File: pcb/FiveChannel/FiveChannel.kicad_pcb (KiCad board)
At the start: 2 copper layers, 79.8 x 76 mm, 29 parts, among them J101 UPDI, J102 5V In, J201 Power Out, J202 NeoPixel Data, J203 Power Out, J204 NeoPixel Data, J205 Power Out, J206 NeoPixel Data, J207 Power Out, J208 NeoPixel Data, J209 Power Out, J210 NeoPixel Data, U101 74LS596, U102 ATTINY1614

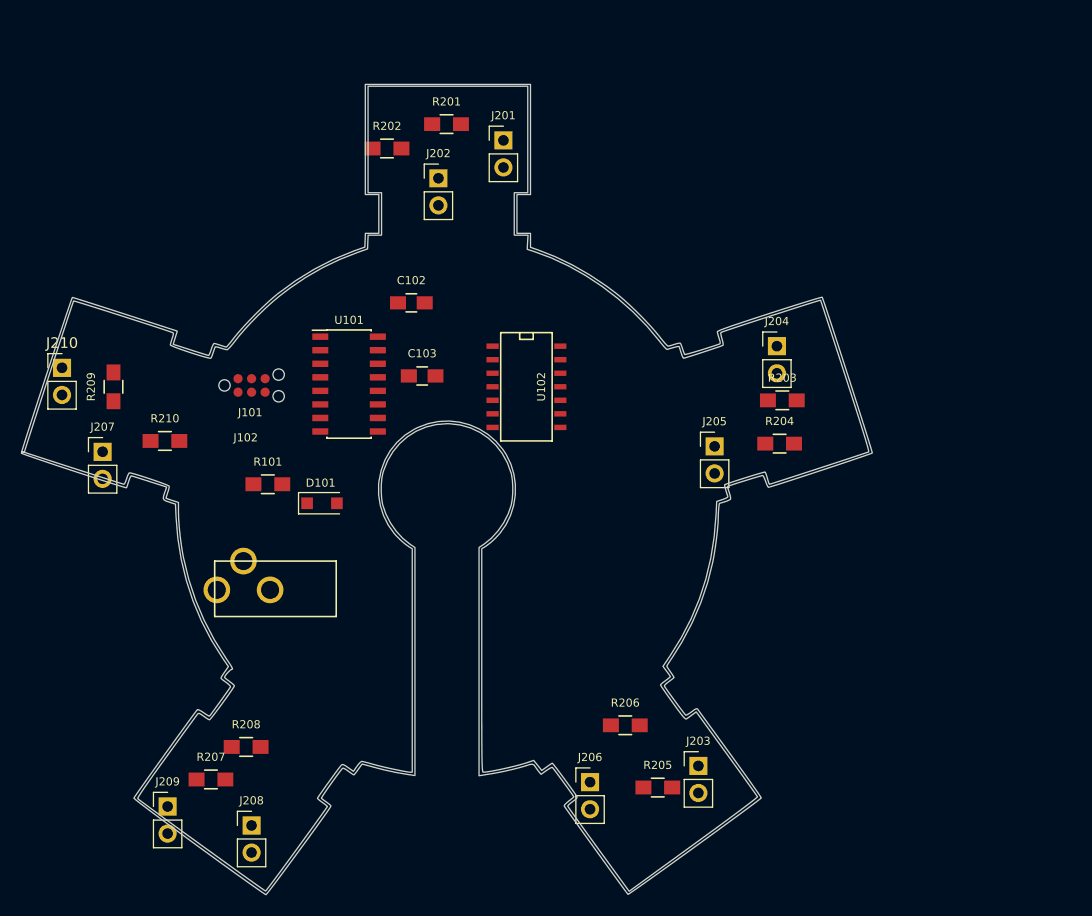
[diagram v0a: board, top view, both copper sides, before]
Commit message: Working through the five channel prototype layout
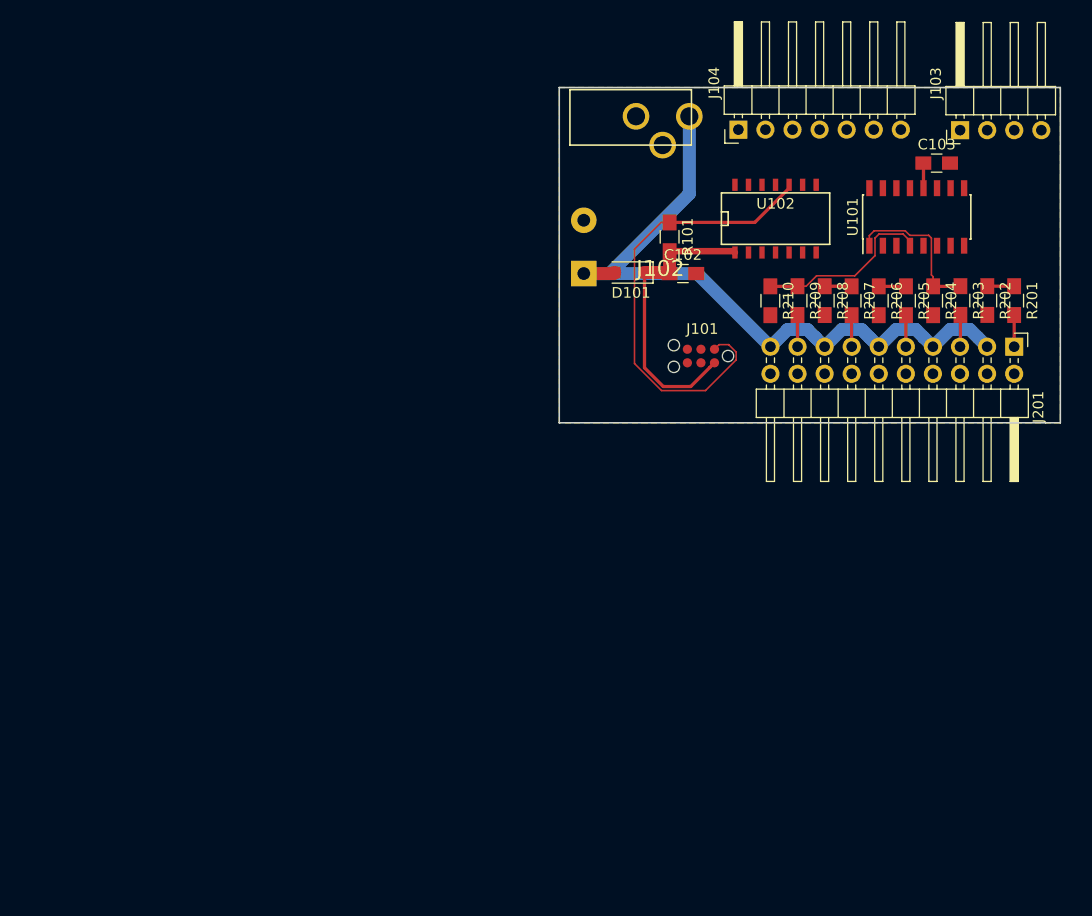
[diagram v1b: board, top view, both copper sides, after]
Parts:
- removed G***: LOGO, advent_sternla:EdgeCut_5
- removed J202, J204, J206, J208, J210: NeoPixel Data, Pin_Headers:Pin_Header_Straight_1x02_Pitch2.54mm
- removed J203, J205, J207, J209: Power Out, Pin_Headers:Pin_Header_Straight_1x02_Pitch2.54mm
- added C101: 1000μF 25V, advent_sternla:CP_Radial_L21.0mm_D13.0mm_P5.00mm_Horizontal, B.Cu at (128.9, 64.3)
- added J103: Conn_01x04_Male, Pin_Headers:Pin_Header_Angled_1x04_Pitch2.54mm, F.Cu at (164.2, 53.4)
- added J104: Conn_01x07_Male, Pin_Headers:Pin_Header_Angled_1x07_Pitch2.54mm, F.Cu at (143.4, 53.4)
- J201: value Power Out -> Conn_01x20_Male; footprint Pin_Headers:Pin_Header_Straight_1x02_Pitch2.54mm -> Pin_Headers:Pin_Header_Angled_2x10_Pitch2.54mm
- moved R207 75.0 mm to (154.1, 69.4), turned to 270 degrees
- moved R208 68.5 mm to (151.6, 69.4), turned to 270 degrees
- moved R209 64.7 mm to (149.0, 69.4), turned to 270 degrees
- moved J102 59.3 mm to (136.3, 52.1), turned to 0 degrees
- moved R210 58.3 mm to (146.4, 69.4), turned to 270 degrees
- moved R202 58.1 mm to (166.8, 69.4), turned to 270 degrees
- moved R201 55.8 mm to (169.3, 69.4), turned to 270 degrees
- moved U101 55.5 mm to (160.2, 61.5), turned to 90 degrees
- moved C103 52.2 mm to (162.1, 56.5)
- moved J201 51.7 mm to (169.3, 73.7), turned to 270 degrees
- moved R205 51.3 mm to (159.2, 69.4), turned to 270 degrees
- moved R206 46.4 mm to (156.6, 69.4), turned to 270 degrees
- moved J101 44.9 mm to (141.2, 73.9), turned to 180 degrees
- moved R101 44.3 mm to (137.0, 63.4), turned to 270 degrees
- moved D101 36.1 mm to (133.2, 66.8), turned to 180 degrees
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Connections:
- J201 pad 1: /VDD -> /Channels/NP_DATA_0
- U102 pad 3: (no net) -> /PA5
- U102 pad 4: (no net) -> /PA6
- U102 pad 5: (no net) -> /PA7
- U102 pad 6: (no net) -> /PB3
- U102 pad 7: (no net) -> /PB2
- U102 pad 8: (no net) -> /PB1
- U102 pad 9: (no net) -> /PB0
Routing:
- net /5V: track 0.00 -> 69.2 mm
- net /PDI_DATA: track 0.00 -> 43.0 mm
- net /VDD: track 0.00 -> 27.8 mm
- net /CHANNEL_4: track 0.00 -> 16.8 mm
- net /CHANNEL_1: track 0.00 -> 14.4 mm
- net /CHANNEL_3: track 0.00 -> 3.38 mm
- net /CHANNEL_2: track 0.00 -> 3.09 mm
- net /Channels/NP_DATA_1: track 0.00 -> 3.05 mm
- net /Channels/NP_DATA_3: track 0.00 -> 2.98 mm
- net /Channels/NP_DATA_2: track 0.00 -> 2.98 mm
- net /Channels/NP_DATA_4: track 0.00 -> 2.97 mm
- net /Channels/NP_DATA_0: track 0.00 -> 2.97 mm
- net /CHANNEL_0: track 0.00 -> 2.52 mm
- net /LATCH_PIN: track 0.00 -> 2.36 mm
- added copper zone on F.Cu, net GND
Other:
- board size 79.8 x 76 mm -> 47 x 31.4 mm

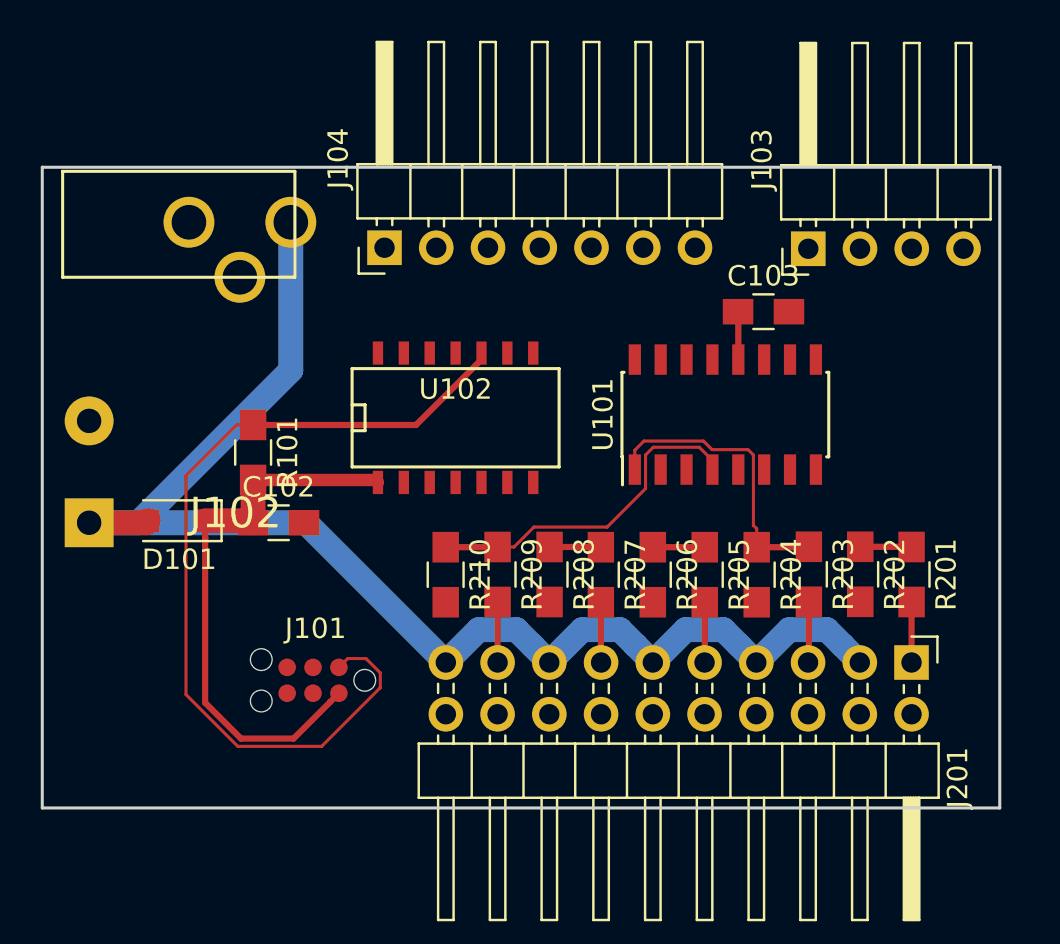
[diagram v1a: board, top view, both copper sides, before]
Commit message: Finished the layout and sent to OSH Park
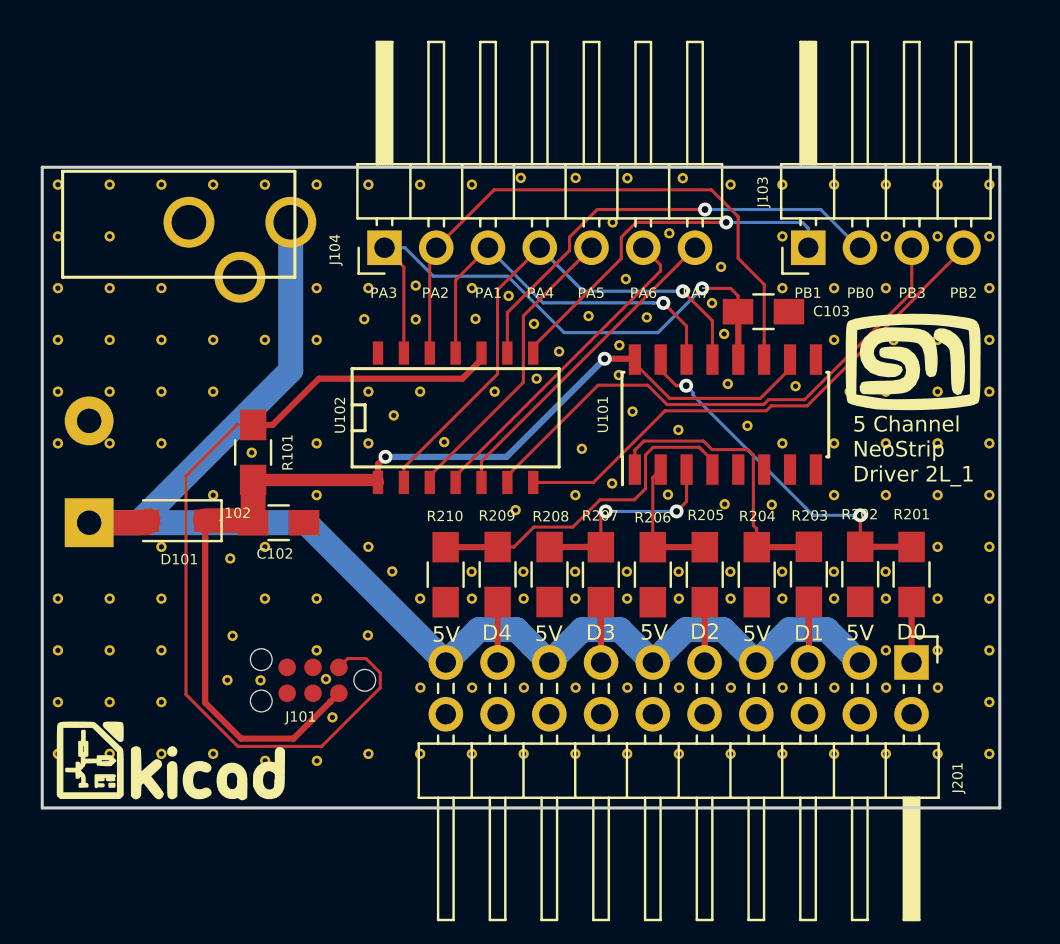
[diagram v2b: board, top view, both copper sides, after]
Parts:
- added G***: LOGO, advent_sternla:MyBasic_rounded_50_1, B.Cu at (157.0, 64.3)
- added G***: LOGO, advent_sternla:KiCad-Logo, F.Cu at (133.0, 78.5)
- added G***: LOGO, advent_sternla:MyBasic_rounded_50_1, F.Cu at (169.4, 58.9)
- added REF***: KiCad-Logo2_6mm_SilkScreen, Symbols:KiCad-Logo2_6mm_SilkScreen, B.Cu at (169.6, 64.2)
- added ST**: STITCH_VIA, advent_sternla:STITCH_VIA, F.Cu at (135.7, 74.6)
- added ST**: STITCH_VIA, advent_sternla:STITCH_VIA, F.Cu at (157.9, 78.2)
- added ST**: STITCH_VIA, advent_sternla:STITCH_VIA, F.Cu at (161.3, 62.1)
- added ST**: STITCH_VIA, advent_sternla:STITCH_VIA, F.Cu at (157.9, 62.3)
- added ST**: STITCH_VIA, advent_sternla:STITCH_VIA, F.Cu at (155.6, 61.4)
- added ST**: STITCH_VIA, advent_sternla:STITCH_VIA, F.Cu at (153.1, 63.2)
- added ST**: STITCH_VIA, advent_sternla:STITCH_VIA, F.Cu at (146.4, 62.9)
- added ST**: STITCH_VIA, advent_sternla:STITCH_VIA, F.Cu at (142.7, 63.0)
- added ST**: STITCH_VIA, advent_sternla:STITCH_VIA, F.Cu at (140.1, 63.0)
- added ST**: STITCH_VIA, advent_sternla:STITCH_VIA, F.Cu at (136.9, 63.4)
- added ST**: STITCH_VIA, advent_sternla:STITCH_VIA, F.Cu at (132.5, 63.0)
- added ST**: STITCH_VIA, advent_sternla:STITCH_VIA, F.Cu at (130.0, 63.0)
- added ST**: STITCH_VIA, advent_sternla:STITCH_VIA, F.Cu at (155.4, 78.2)
- added ST**: STITCH_VIA, advent_sternla:STITCH_VIA, F.Cu at (127.4, 63.0)
- added ST**: STITCH_VIA, advent_sternla:STITCH_VIA, F.Cu at (173.1, 60.4)
- added ST**: STITCH_VIA, advent_sternla:STITCH_VIA, F.Cu at (170.6, 60.4)
- added ST**: STITCH_VIA, advent_sternla:STITCH_VIA, F.Cu at (168.1, 60.4)
- added ST**: STITCH_VIA, advent_sternla:STITCH_VIA, F.Cu at (166.3, 60.4)
- added ST**: STITCH_VIA, advent_sternla:STITCH_VIA, F.Cu at (163.6, 60.1)
- added ST**: STITCH_VIA, advent_sternla:STITCH_VIA, F.Cu at (160.3, 60.0)
- added ST**: STITCH_VIA, advent_sternla:STITCH_VIA, F.Cu at (150.9, 59.8)
- added ST**: STITCH_VIA, advent_sternla:STITCH_VIA, F.Cu at (148.9, 60.4)
- added ST**: STITCH_VIA, advent_sternla:STITCH_VIA, F.Cu at (145.2, 60.4)
- added ST**: STITCH_VIA, advent_sternla:STITCH_VIA, F.Cu at (152.8, 78.2)
- added ST**: STITCH_VIA, advent_sternla:STITCH_VIA, F.Cu at (142.7, 60.4)
- added ST**: STITCH_VIA, advent_sternla:STITCH_VIA, F.Cu at (135.0, 60.4)
- added ST**: STITCH_VIA, advent_sternla:STITCH_VIA, F.Cu at (132.5, 60.4)
- added ST**: STITCH_VIA, advent_sternla:STITCH_VIA, F.Cu at (130.0, 60.4)
- added ST**: STITCH_VIA, advent_sternla:STITCH_VIA, F.Cu at (127.4, 60.4)
- added ST**: STITCH_VIA, advent_sternla:STITCH_VIA, F.Cu at (173.1, 57.9)
- added ST**: STITCH_VIA, advent_sternla:STITCH_VIA, F.Cu at (170.6, 57.9)
- added ST**: STITCH_VIA, advent_sternla:STITCH_VIA, F.Cu at (168.4, 57.9)
- added ST**: STITCH_VIA, advent_sternla:STITCH_VIA, F.Cu at (165.5, 57.9)
- added ST**: STITCH_VIA, advent_sternla:STITCH_VIA, F.Cu at (160.1, 57.6)
- added ST**: STITCH_VIA, advent_sternla:STITCH_VIA, F.Cu at (150.3, 78.2)
- added ST**: STITCH_VIA, advent_sternla:STITCH_VIA, F.Cu at (155.0, 58.1)
- added ST**: STITCH_VIA, advent_sternla:STITCH_VIA, F.Cu at (152.0, 58.4)
- added ST**: STITCH_VIA, advent_sternla:STITCH_VIA, F.Cu at (150.8, 57.1)
- added ST**: STITCH_VIA, advent_sternla:STITCH_VIA, F.Cu at (147.9, 56.8)
- added ST**: STITCH_VIA, advent_sternla:STITCH_VIA, F.Cu at (145.0, 56.9)
- added ST**: STITCH_VIA, advent_sternla:STITCH_VIA, F.Cu at (142.5, 56.9)
- added ST**: STITCH_VIA, advent_sternla:STITCH_VIA, F.Cu at (140.1, 57.9)
- added ST**: STITCH_VIA, advent_sternla:STITCH_VIA, F.Cu at (137.6, 57.9)
- added ST**: STITCH_VIA, advent_sternla:STITCH_VIA, F.Cu at (135.0, 57.9)
- added ST**: STITCH_VIA, advent_sternla:STITCH_VIA, F.Cu at (132.5, 57.9)
- added ST**: STITCH_VIA, advent_sternla:STITCH_VIA, F.Cu at (147.7, 78.2)
- added ST**: STITCH_VIA, advent_sternla:STITCH_VIA, F.Cu at (130.0, 57.9)
- added ST**: STITCH_VIA, advent_sternla:STITCH_VIA, F.Cu at (127.4, 57.9)
- added ST**: STITCH_VIA, advent_sternla:STITCH_VIA, F.Cu at (173.1, 55.3)
- added ST**: STITCH_VIA, advent_sternla:STITCH_VIA, F.Cu at (168.1, 55.3)
- added ST**: STITCH_VIA, advent_sternla:STITCH_VIA, F.Cu at (165.5, 55.3)
- added ST**: STITCH_VIA, advent_sternla:STITCH_VIA, F.Cu at (163.0, 55.3)
- added ST**: STITCH_VIA, advent_sternla:STITCH_VIA, F.Cu at (159.5, 56.1)
- added ST**: STITCH_VIA, advent_sternla:STITCH_VIA, F.Cu at (156.3, 56.8)
- added ST**: STITCH_VIA, advent_sternla:STITCH_VIA, F.Cu at (155.3, 54.9)
- added ST**: STITCH_VIA, advent_sternla:STITCH_VIA, F.Cu at (153.5, 56.7)
- added ST**: STITCH_VIA, advent_sternla:STITCH_VIA, F.Cu at (145.2, 78.2)
- added ST**: STITCH_VIA, advent_sternla:STITCH_VIA, F.Cu at (149.5, 55.7)
- added ST**: STITCH_VIA, advent_sternla:STITCH_VIA, F.Cu at (147.7, 55.3)
- added ST**: STITCH_VIA, advent_sternla:STITCH_VIA, F.Cu at (145.0, 55.2)
- added ST**: STITCH_VIA, advent_sternla:STITCH_VIA, F.Cu at (142.7, 55.3)
- added ST**: STITCH_VIA, advent_sternla:STITCH_VIA, F.Cu at (140.1, 55.3)
- added ST**: STITCH_VIA, advent_sternla:STITCH_VIA, F.Cu at (154.6, 52.1)
- added ST**: STITCH_VIA, advent_sternla:STITCH_VIA, F.Cu at (157.4, 52.6)
- added ST**: STITCH_VIA, advent_sternla:STITCH_VIA, F.Cu at (132.5, 55.3)
- added ST**: STITCH_VIA, advent_sternla:STITCH_VIA, F.Cu at (130.0, 55.3)
- added ST**: STITCH_VIA, advent_sternla:STITCH_VIA, F.Cu at (127.4, 55.3)
- added ST**: STITCH_VIA, advent_sternla:STITCH_VIA, F.Cu at (142.7, 78.2)
- added ST**: STITCH_VIA, advent_sternla:STITCH_VIA, F.Cu at (173.1, 52.8)
- added ST**: STITCH_VIA, advent_sternla:STITCH_VIA, F.Cu at (170.6, 52.8)
- added ST**: STITCH_VIA, advent_sternla:STITCH_VIA, F.Cu at (168.1, 52.8)
- added ST**: STITCH_VIA, advent_sternla:STITCH_VIA, F.Cu at (163.0, 52.8)
- added ST**: STITCH_VIA, advent_sternla:STITCH_VIA, F.Cu at (160.0, 54.3)
- added ST**: STITCH_VIA, advent_sternla:STITCH_VIA, F.Cu at (130.0, 52.8)
- added ST**: STITCH_VIA, advent_sternla:STITCH_VIA, F.Cu at (127.4, 52.8)
- added ST**: STITCH_VIA, advent_sternla:STITCH_VIA, F.Cu at (173.1, 50.3)
- added ST**: STITCH_VIA, advent_sternla:STITCH_VIA, F.Cu at (170.6, 50.3)
- added ST**: STITCH_VIA, advent_sternla:STITCH_VIA, F.Cu at (168.1, 50.3)
- added ST**: STITCH_VIA, advent_sternla:STITCH_VIA, F.Cu at (140.1, 78.5)
- added ST**: STITCH_VIA, advent_sternla:STITCH_VIA, F.Cu at (165.5, 50.3)
- added ST**: STITCH_VIA, advent_sternla:STITCH_VIA, F.Cu at (163.0, 50.3)
- added ST**: STITCH_VIA, advent_sternla:STITCH_VIA, F.Cu at (160.4, 50.3)
- added ST**: STITCH_VIA, advent_sternla:STITCH_VIA, F.Cu at (158.1, 49.9)
- added ST**: STITCH_VIA, advent_sternla:STITCH_VIA, F.Cu at (155.4, 49.9)
- added ST**: STITCH_VIA, advent_sternla:STITCH_VIA, F.Cu at (152.8, 49.9)
- added ST**: STITCH_VIA, advent_sternla:STITCH_VIA, F.Cu at (150.1, 49.9)
- added ST**: STITCH_VIA, advent_sternla:STITCH_VIA, F.Cu at (147.7, 50.3)
- added ST**: STITCH_VIA, advent_sternla:STITCH_VIA, F.Cu at (145.2, 50.3)
- added ST**: STITCH_VIA, advent_sternla:STITCH_VIA, F.Cu at (142.7, 50.3)
- added ST**: STITCH_VIA, advent_sternla:STITCH_VIA, F.Cu at (137.6, 78.5)
- added ST**: STITCH_VIA, advent_sternla:STITCH_VIA, F.Cu at (140.1, 50.3)
- added ST**: STITCH_VIA, advent_sternla:STITCH_VIA, F.Cu at (137.6, 50.3)
- added ST**: STITCH_VIA, advent_sternla:STITCH_VIA, F.Cu at (135.0, 50.3)
- added ST**: STITCH_VIA, advent_sternla:STITCH_VIA, F.Cu at (132.5, 50.3)
- added ST**: STITCH_VIA, advent_sternla:STITCH_VIA, F.Cu at (130.0, 50.3)
- added ST**: STITCH_VIA, advent_sternla:STITCH_VIA, F.Cu at (127.4, 50.3)
- added ST**: STITCH_VIA, advent_sternla:STITCH_VIA, F.Cu at (135.0, 78.2)
- added ST**: STITCH_VIA, advent_sternla:STITCH_VIA, F.Cu at (155.0, 59.6)
- added ST**: STITCH_VIA, advent_sternla:STITCH_VIA, F.Cu at (132.5, 78.2)
- added ST**: STITCH_VIA, advent_sternla:STITCH_VIA, F.Cu at (130.0, 78.2)
- added ST**: STITCH_VIA, advent_sternla:STITCH_VIA, F.Cu at (127.4, 78.2)
- added ST**: STITCH_VIA, advent_sternla:STITCH_VIA, F.Cu at (173.1, 75.7)
- added ST**: STITCH_VIA, advent_sternla:STITCH_VIA, F.Cu at (170.6, 74.9)
- added ST**: STITCH_VIA, advent_sternla:STITCH_VIA, F.Cu at (168.1, 74.9)
- added ST**: STITCH_VIA, advent_sternla:STITCH_VIA, F.Cu at (165.5, 74.9)
- added ST**: STITCH_VIA, advent_sternla:STITCH_VIA, F.Cu at (163.0, 74.9)
- added ST**: STITCH_VIA, advent_sternla:STITCH_VIA, F.Cu at (160.5, 74.9)
- added ST**: STITCH_VIA, advent_sternla:STITCH_VIA, F.Cu at (157.9, 74.9)
- added ST**: STITCH_VIA, advent_sternla:STITCH_VIA, F.Cu at (143.9, 61.6)
- added ST**: STITCH_VIA, advent_sternla:STITCH_VIA, F.Cu at (155.4, 74.9)
- added ST**: STITCH_VIA, advent_sternla:STITCH_VIA, F.Cu at (152.8, 74.9)
- added ST**: STITCH_VIA, advent_sternla:STITCH_VIA, F.Cu at (150.3, 74.9)
- added ST**: STITCH_VIA, advent_sternla:STITCH_VIA, F.Cu at (147.8, 74.9)
- added ST**: STITCH_VIA, advent_sternla:STITCH_VIA, F.Cu at (145.2, 74.9)
- added ST**: STITCH_VIA, advent_sternla:STITCH_VIA, F.Cu at (140.9, 76.4)
- added ST**: STITCH_VIA, advent_sternla:STITCH_VIA, F.Cu at (140.6, 74.5)
- added ST**: STITCH_VIA, advent_sternla:STITCH_VIA, F.Cu at (136.0, 72.4)
- added ST**: STITCH_VIA, advent_sternla:STITCH_VIA, F.Cu at (132.5, 75.7)
- added ST**: STITCH_VIA, advent_sternla:STITCH_VIA, F.Cu at (130.0, 75.7)
- added ST**: STITCH_VIA, advent_sternla:STITCH_VIA, F.Cu at (173.1, 78.2)
- added ST**: STITCH_VIA, advent_sternla:STITCH_VIA, F.Cu at (127.4, 75.7)
- added ST**: STITCH_VIA, advent_sternla:STITCH_VIA, F.Cu at (173.1, 73.1)
- added ST**: STITCH_VIA, advent_sternla:STITCH_VIA, F.Cu at (170.6, 73.1)
- added ST**: STITCH_VIA, advent_sternla:STITCH_VIA, F.Cu at (168.1, 73.1)
- added ST**: STITCH_VIA, advent_sternla:STITCH_VIA, F.Cu at (142.6, 72.4)
- added ST**: STITCH_VIA, advent_sternla:STITCH_VIA, F.Cu at (140.1, 73.1)
- added ST**: STITCH_VIA, advent_sternla:STITCH_VIA, F.Cu at (137.4, 74.6)
- added ST**: STITCH_VIA, advent_sternla:STITCH_VIA, F.Cu at (132.5, 73.1)
- added ST**: STITCH_VIA, advent_sternla:STITCH_VIA, F.Cu at (130.0, 73.1)
- added ST**: STITCH_VIA, advent_sternla:STITCH_VIA, F.Cu at (127.4, 73.1)
- added ST**: STITCH_VIA, advent_sternla:STITCH_VIA, F.Cu at (170.6, 78.2)
- added ST**: STITCH_VIA, advent_sternla:STITCH_VIA, F.Cu at (173.1, 70.6)
- added ST**: STITCH_VIA, advent_sternla:STITCH_VIA, F.Cu at (170.6, 70.6)
- added ST**: STITCH_VIA, advent_sternla:STITCH_VIA, F.Cu at (168.1, 70.6)
- added ST**: STITCH_VIA, advent_sternla:STITCH_VIA, F.Cu at (165.5, 70.6)
- added ST**: STITCH_VIA, advent_sternla:STITCH_VIA, F.Cu at (163.0, 70.6)
- added ST**: STITCH_VIA, advent_sternla:STITCH_VIA, F.Cu at (160.4, 70.6)
- added ST**: STITCH_VIA, advent_sternla:STITCH_VIA, F.Cu at (157.9, 70.6)
- added ST**: STITCH_VIA, advent_sternla:STITCH_VIA, F.Cu at (155.4, 70.6)
- added ST**: STITCH_VIA, advent_sternla:STITCH_VIA, F.Cu at (152.8, 70.6)
- added ST**: STITCH_VIA, advent_sternla:STITCH_VIA, F.Cu at (150.3, 70.6)
- added ST**: STITCH_VIA, advent_sternla:STITCH_VIA, F.Cu at (168.1, 78.2)
- added ST**: STITCH_VIA, advent_sternla:STITCH_VIA, F.Cu at (147.7, 70.6)
- added ST**: STITCH_VIA, advent_sternla:STITCH_VIA, F.Cu at (145.2, 70.6)
- added ST**: STITCH_VIA, advent_sternla:STITCH_VIA, F.Cu at (140.1, 70.6)
- added ST**: STITCH_VIA, advent_sternla:STITCH_VIA, F.Cu at (137.6, 70.6)
- added ST**: STITCH_VIA, advent_sternla:STITCH_VIA, F.Cu at (132.5, 70.6)
- added ST**: STITCH_VIA, advent_sternla:STITCH_VIA, F.Cu at (130.0, 70.6)
- added ST**: STITCH_VIA, advent_sternla:STITCH_VIA, F.Cu at (127.4, 70.6)
- added ST**: STITCH_VIA, advent_sternla:STITCH_VIA, F.Cu at (173.1, 68.0)
- added ST**: STITCH_VIA, advent_sternla:STITCH_VIA, F.Cu at (170.6, 68.0)
- added ST**: STITCH_VIA, advent_sternla:STITCH_VIA, F.Cu at (168.0, 69.3)
- added ST**: STITCH_VIA, advent_sternla:STITCH_VIA, F.Cu at (165.5, 78.2)
- added ST**: STITCH_VIA, advent_sternla:STITCH_VIA, F.Cu at (165.5, 69.3)
- added ST**: STITCH_VIA, advent_sternla:STITCH_VIA, F.Cu at (163.0, 69.3)
- added ST**: STITCH_VIA, advent_sternla:STITCH_VIA, F.Cu at (160.4, 69.3)
- added ST**: STITCH_VIA, advent_sternla:STITCH_VIA, F.Cu at (157.9, 69.3)
- added ST**: STITCH_VIA, advent_sternla:STITCH_VIA, F.Cu at (155.3, 69.3)
- added ST**: STITCH_VIA, advent_sternla:STITCH_VIA, F.Cu at (152.8, 69.3)
- added ST**: STITCH_VIA, advent_sternla:STITCH_VIA, F.Cu at (150.3, 69.3)
- added ST**: STITCH_VIA, advent_sternla:STITCH_VIA, F.Cu at (147.7, 69.3)
- added ST**: STITCH_VIA, advent_sternla:STITCH_VIA, F.Cu at (143.8, 69.2)
- added ST**: STITCH_VIA, advent_sternla:STITCH_VIA, F.Cu at (142.7, 68.0)
- added ST**: STITCH_VIA, advent_sternla:STITCH_VIA, F.Cu at (163.0, 78.2)
- added ST**: STITCH_VIA, advent_sternla:STITCH_VIA, F.Cu at (137.6, 68.0)
- added ST**: STITCH_VIA, advent_sternla:STITCH_VIA, F.Cu at (135.9, 68.6)
- added ST**: STITCH_VIA, advent_sternla:STITCH_VIA, F.Cu at (132.5, 68.0)
- added ST**: STITCH_VIA, advent_sternla:STITCH_VIA, F.Cu at (173.1, 65.5)
- added ST**: STITCH_VIA, advent_sternla:STITCH_VIA, F.Cu at (170.6, 65.5)
- added ST**: STITCH_VIA, advent_sternla:STITCH_VIA, F.Cu at (168.1, 65.5)
- added ST**: STITCH_VIA, advent_sternla:STITCH_VIA, F.Cu at (165.5, 65.5)
- added ST**: STITCH_VIA, advent_sternla:STITCH_VIA, F.Cu at (162.5, 66.0)
- added ST**: STITCH_VIA, advent_sternla:STITCH_VIA, F.Cu at (160.1, 65.9)
- added ST**: STITCH_VIA, advent_sternla:STITCH_VIA, F.Cu at (157.4, 65.5)
- added ST**: STITCH_VIA, advent_sternla:STITCH_VIA, F.Cu at (160.4, 78.2)
- added ST**: STITCH_VIA, advent_sternla:STITCH_VIA, F.Cu at (154.6, 64.9)
- added ST**: STITCH_VIA, advent_sternla:STITCH_VIA, F.Cu at (152.8, 65.5)
- added ST**: STITCH_VIA, advent_sternla:STITCH_VIA, F.Cu at (149.9, 66.2)
- added ST**: STITCH_VIA, advent_sternla:STITCH_VIA, F.Cu at (140.1, 65.5)
- added ST**: STITCH_VIA, advent_sternla:STITCH_VIA, F.Cu at (135.0, 65.5)
- added ST**: STITCH_VIA, advent_sternla:STITCH_VIA, F.Cu at (173.1, 63.0)
- added ST**: STITCH_VIA, advent_sternla:STITCH_VIA, F.Cu at (170.6, 63.0)
- added ST**: STITCH_VIA, advent_sternla:STITCH_VIA, F.Cu at (168.1, 63.0)
- added ST**: STITCH_VIA, advent_sternla:STITCH_VIA, F.Cu at (165.5, 63.0)
- added ST**: STITCH_VIA, advent_sternla:STITCH_VIA, F.Cu at (163.0, 63.0)
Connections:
- J103 pad 1: /PB0 -> /PB1
- J103 pad 2: /PB1 -> /PB0
- J103 pad 3: /PB2 -> /PB3
- J103 pad 4: /PB3 -> /PB2
- J104 pad 1: /DATA_PIN -> /LATCH_PIN
- J104 pad 3: /LATCH_PIN -> /DATA_PIN
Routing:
- net /CLK_PIN: track 0.00 -> 29.4 mm
- net /PB3: track 0.00 -> 26.8 mm
- net /LATCH_PIN: track 2.36 -> 28.9 mm, vias 0 -> 1
- net /~ENABLE: track 0.00 -> 26.1 mm, vias 0 -> 1
- net /PB2: track 0.00 -> 25.9 mm
- net /VDD: track 27.8 -> 53.3 mm, vias 0 -> 2
- net /PB0: track 0.00 -> 22.6 mm, vias 0 -> 1
- net /DATA_PIN: track 0.00 -> 18.8 mm, vias 0 -> 1
- net /PB1: track 0.00 -> 18.1 mm, vias 0 -> 1
- net /PA6: track 0.00 -> 16.0 mm
- net /PA7: track 0.00 -> 15.9 mm
- net /CHANNEL_0: track 2.52 -> 17.9 mm, vias 0 -> 2
- net /PA5: track 0.00 -> 14.8 mm
- net /CHANNEL_3: track 3.38 -> 11.0 mm, vias 0 -> 2
- net /CHANNEL_2: track 3.09 -> 7.06 mm
- added copper zone on B.Cu, net GND
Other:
- board text added: "5 Channel NeoStrip Driver 2L_1"
- board text added: "5V"
- board text added: "D0"
- board text added: "D1"
- board text added: "D2"
- board text added: "D3"
- board text added: "D4"
- board text added: "PA1"
- board text added: "PA2"
- board text added: "PA3"
- board text added: "PA4"
- board text added: "PA5"
- board text added: "PA6"
- board text added: "PA7"
- board text added: "PB0"
- board text added: "PB1"
- board text added: "PB2"
- board text added: "PB3"

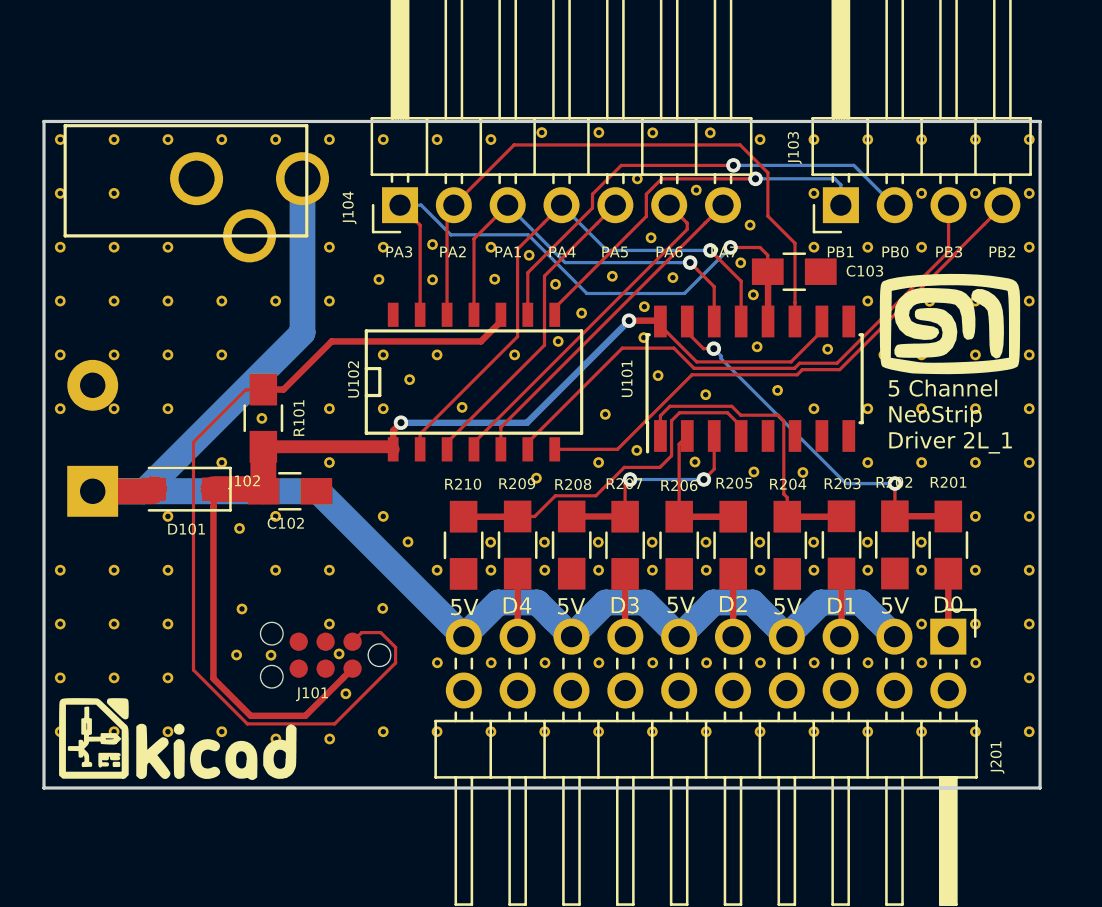
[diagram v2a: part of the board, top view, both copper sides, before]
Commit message: Restores the 5 channel PCB design and updates to KiCad 5
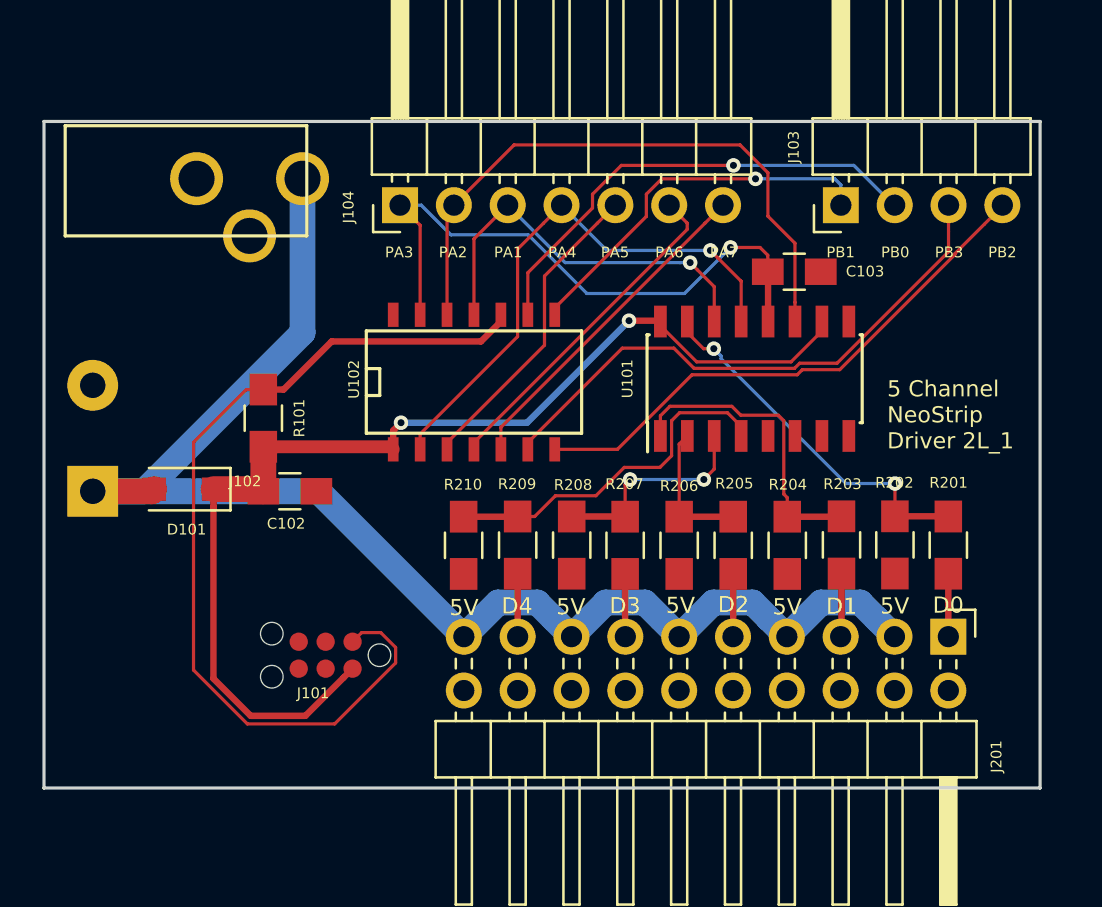
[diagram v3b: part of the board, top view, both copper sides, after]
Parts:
- removed G*** (x2): LOGO, advent_sternla:MyBasic_rounded_50_1
- removed G***: LOGO, advent_sternla:KiCad-Logo
- removed REF***: KiCad-Logo2_6mm_SilkScreen, Symbols:KiCad-Logo2_6mm_SilkScreen
- removed ST** (x185): STITCH_VIA, advent_sternla:STITCH_VIA
- U101: value 74LS596 -> 74LS595
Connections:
- net /~ENABLE renamed /~{ENABLE}
- J101 pad 3: (no net) -> unconnected-(J101-Pin_3-Pad3)
- J101 pad 4: (no net) -> unconnected-(J101-Pin_4-Pad4)
- J101 pad 5: (no net) -> unconnected-(J101-Pin_5-Pad5)
- J102 pad 3: (no net) -> unconnected-(J102-Pad3)
- U101 pad 5: (no net) -> unconnected-(U101-QF-Pad5)
- U101 pad 6: (no net) -> unconnected-(U101-QG-Pad6)
- U101 pad 7: (no net) -> unconnected-(U101-QH-Pad7)
- U101 pad 9: (no net) -> unconnected-(U101-~{QH}-Pad9)
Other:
- net class Default removed
